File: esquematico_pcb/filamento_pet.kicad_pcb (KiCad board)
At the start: 2 copper layers, 150 x 50 mm, 31 parts, among them J1 01x02M, J10 01x03M, J11 01x02M, J12 01x04M, J13 01x02M, J2 01x02M, J3 01x02M, J4 01x02M, J5 01x02M, J6 01x03M, J7 01x03M, J8 01x02M, J9 01x04M, P1 Digital, P2 Analog, Q1 IRF540N, Q2 IRF540N

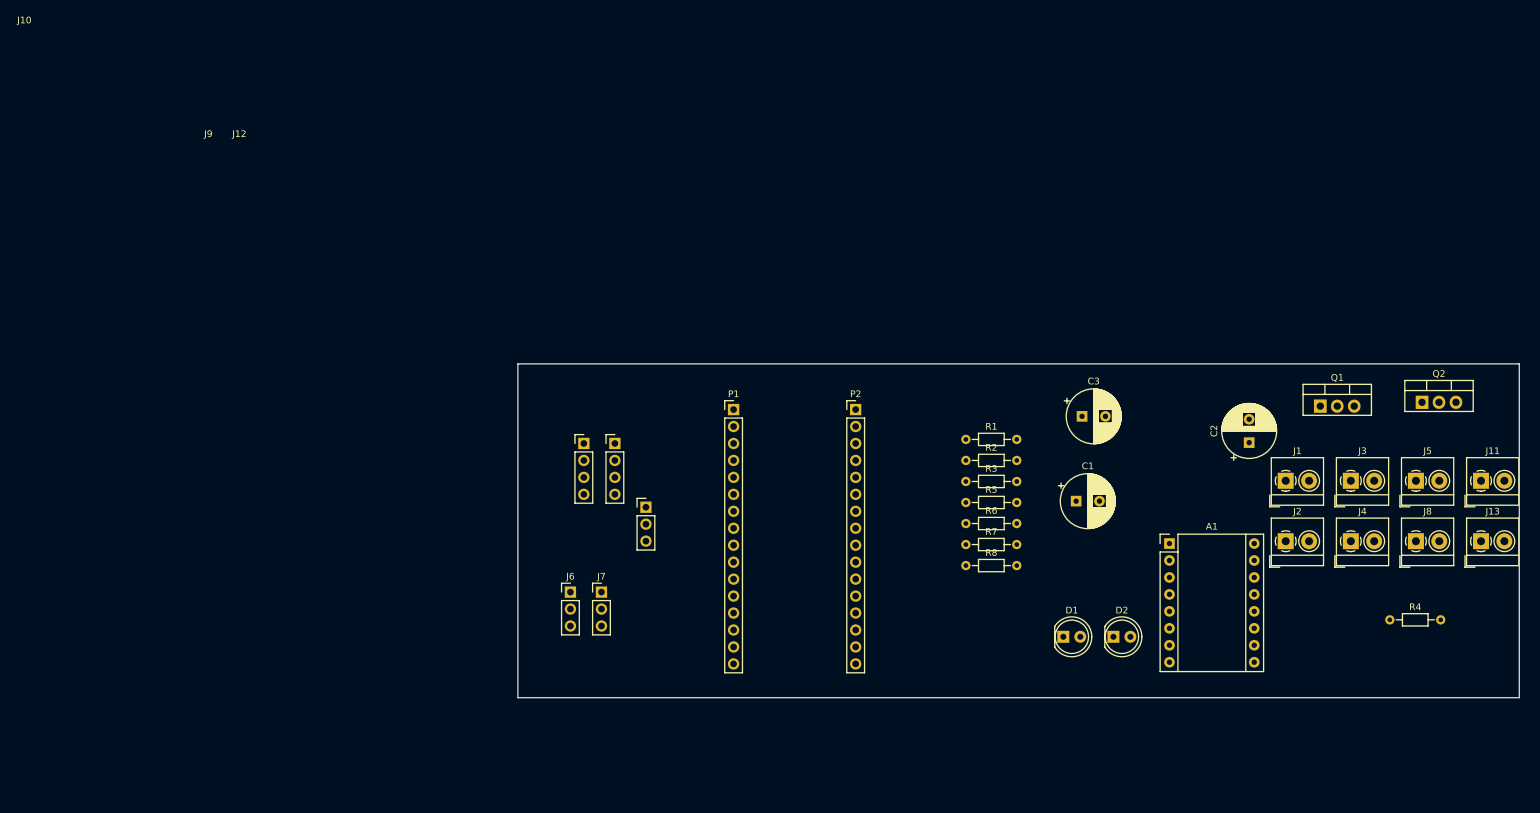
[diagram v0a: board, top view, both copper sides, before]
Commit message: Cambio de footprint Arduino Nano. Conector para encoder (Opcional). 2 Botones
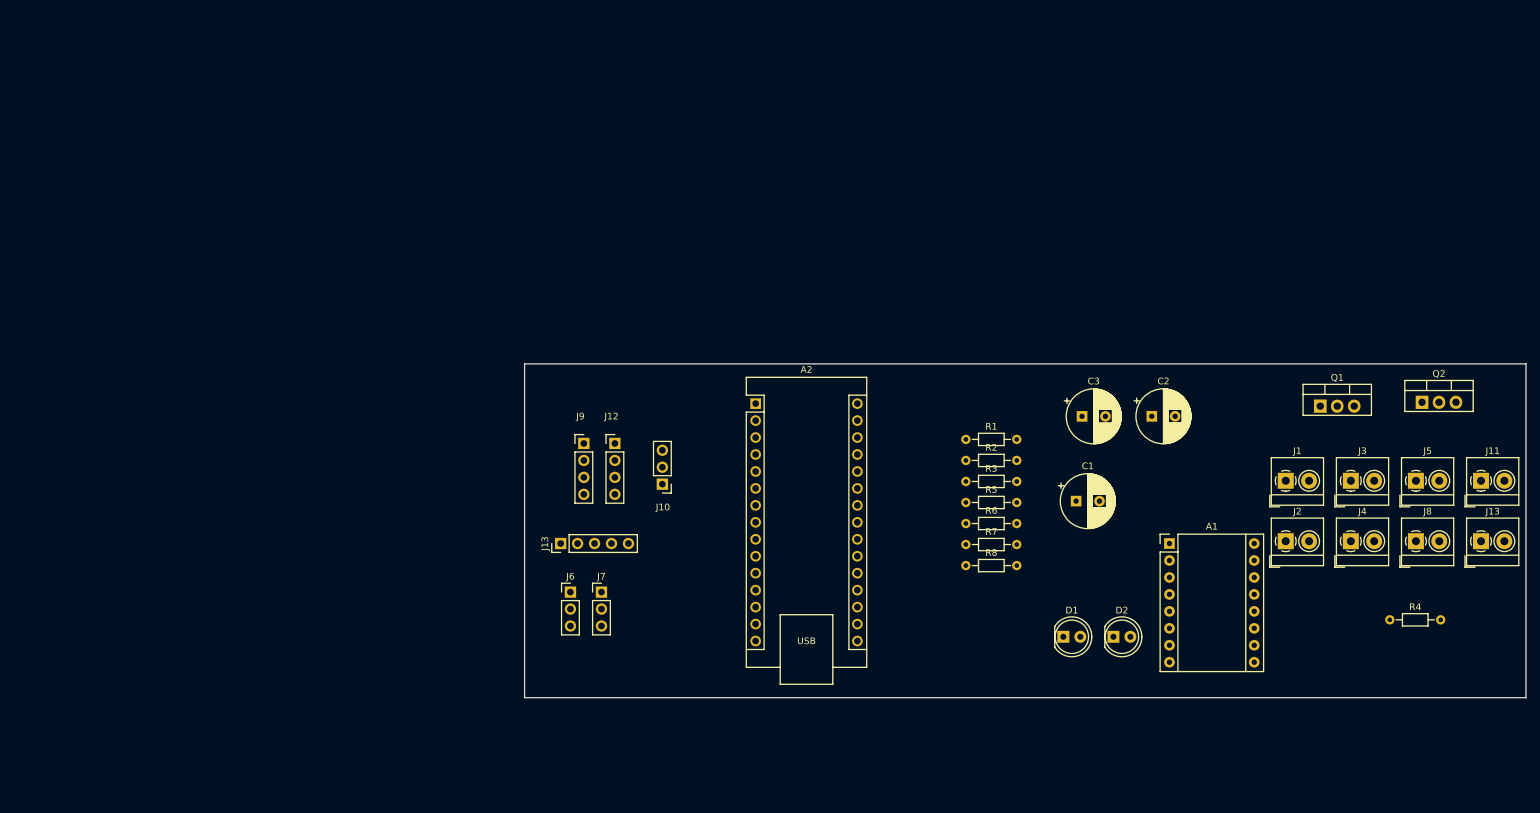
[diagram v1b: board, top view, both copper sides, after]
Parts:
- removed P1: Digital, Connector_PinHeader_2.54mm:PinHeader_1x16_P2.54mm_Vertical
- removed P2: Analog, Connector_PinHeader_2.54mm:PinHeader_1x16_P2.54mm_Vertical
- added A2: Arduino_Nano_v3.x, Module:Arduino_Nano, F.Cu at (54.6, 21.0)
- added J13: Conn_01x05_Pin, Connector_PinHeader_2.54mm:PinHeader_1x05_P2.54mm_Vertical, F.Cu at (25.4, 41.9)
- R1, R4: value R -> 1K8
- R2, R5: value R -> 10R
- R3, R6, R8: value R -> 10K
- R7: value R -> 4K7
- moved C2 15.1 mm to (113.9, 22.9), turned to 0 degrees
- moved J10 4.24 mm to (40.6, 33.0), turned to 180 degrees

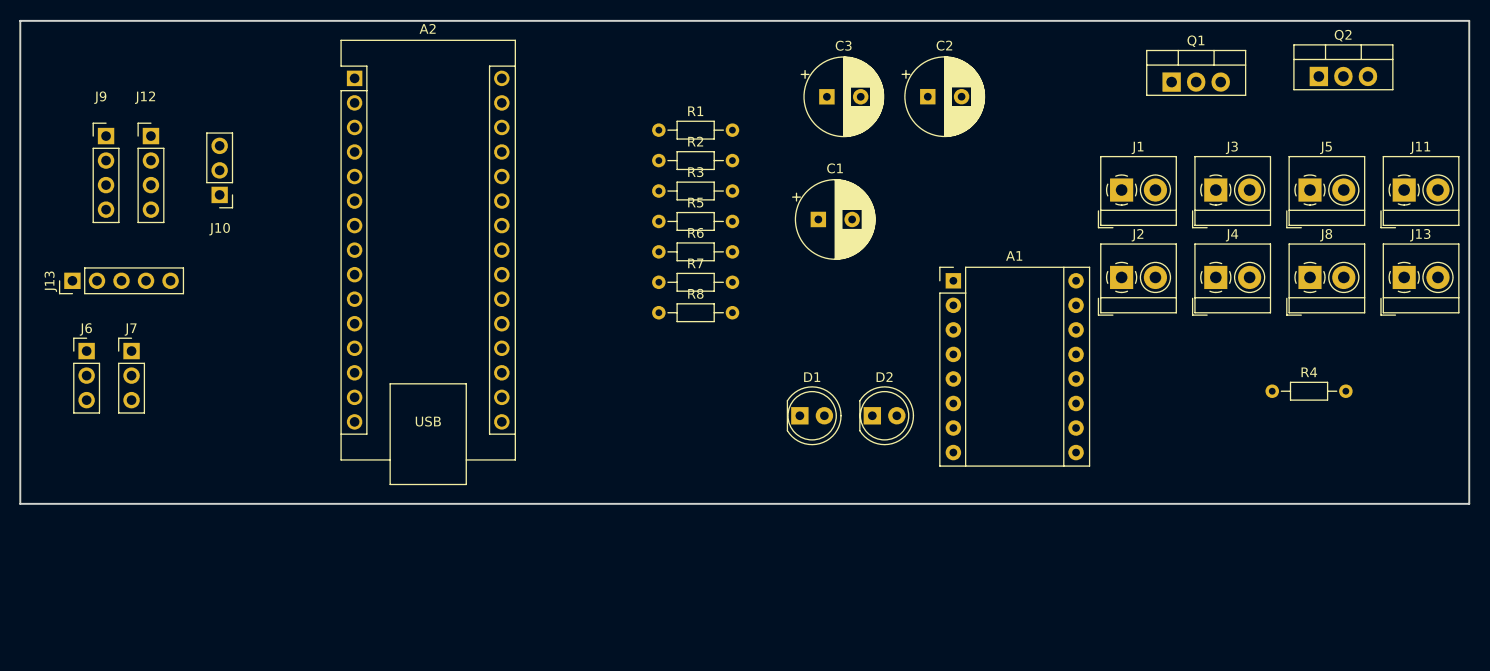
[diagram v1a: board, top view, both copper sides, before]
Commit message: PCB V1.0.0
Agregué LM7805
Cambios pequeños en el esquemático
V1.0.0 del PCB
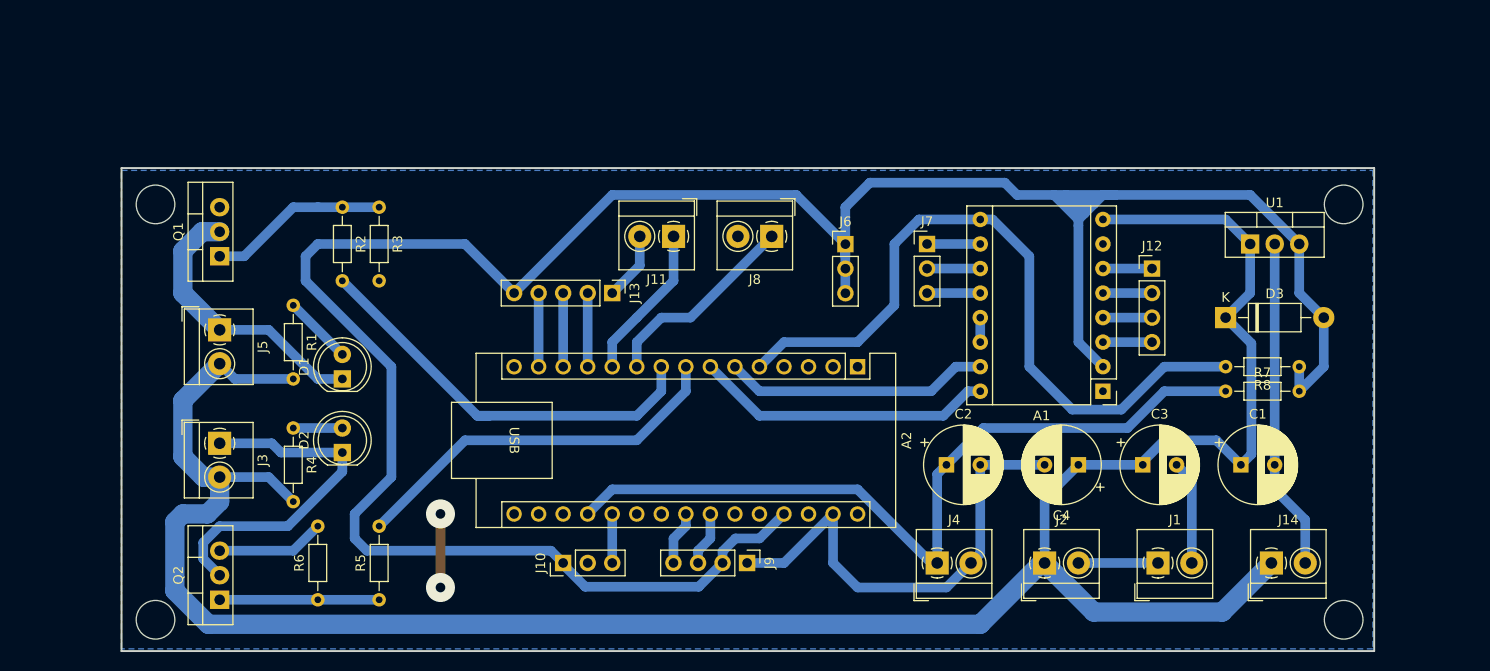
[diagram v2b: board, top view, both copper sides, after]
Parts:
- removed the J13 at (163.3, 41.6)
- removed the J13 at (25.4, 41.9)
- added C4: 10uf, Capacitor_THT:CP_Radial_D8.0mm_P3.50mm, F.Cu at (129.5, 61.0)
- added D3: 1N4007, Diode_THT:D_DO-41_SOD81_P10.16mm_Horizontal, F.Cu at (144.8, 45.7)
- added J13: Conn_01x05_Pin, Connector_PinHeader_2.54mm:PinHeader_1x05_P2.54mm_Vertical, F.Cu at (81.3, 43.2)
- added J14: 01x02M, TerminalBlock_4Ucon:TerminalBlock_4Ucon_1x02_P3.50mm_Horizontal, F.Cu at (149.5, 71.1)
- added U1: LM7805_TO220, Package_TO_SOT_THT:TO-220-3_Vertical, F.Cu at (147.3, 38.1)
- moved Q2 126.0 mm to (40.6, 74.9), turned to 90 degrees
- moved J5 113.8 mm to (40.6, 47.0), turned to -90 degrees
- moved J3 106.4 mm to (40.6, 58.7), turned to -90 degrees
- moved J12 104.5 mm to (137.2, 40.6)
- moved R4 101.4 mm to (48.3, 57.1), turned to -90 degrees
- moved Q1 100.2 mm to (40.6, 39.4), turned to 90 degrees
- moved J7 83.1 mm to (113.9, 38.1)
- moved J9 79.7 mm to (95.2, 71.1), turned to -90 degrees
- moved J6 79.3 mm to (105.4, 38.1)
- moved J11 75.8 mm to (87.6, 37.3), turned to 180 degrees
- moved R8 66.5 mm to (152.4, 50.8), turned to 180 degrees
- moved A2 60.0 mm to (106.7, 50.8), turned to -90 degrees
- moved R7 59.7 mm to (144.8, 53.3)
- moved J8 55.9 mm to (97.8, 37.3), turned to 180 degrees
- moved D2 55.0 mm to (53.3, 59.7), turned to 90 degrees
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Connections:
- A2 pad 4: GND -> unconnected-(A2-GND-Pad4)
- A2 pad 8: MOS -> FAN
- A2 pad 9: FAN -> MOS
- J10 pad 2: Pote_vel -> GND
- J10 pad 3: GND -> Pote_vel
- J11 pad 1: GND -> BUT2
- J11 pad 2: BUT2 -> GND
- J3 pad 1: Net-(D1-K) -> Net-(D2-K)
- J5 pad 1: Net-(D2-K) -> Net-(D1-K)
- J8 pad 1: GND -> BUT1
- J8 pad 2: BUT1 -> GND
- J9 pad 3: SDA -> SCL
- J9 pad 4: SCL -> SDA
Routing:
- net +5V: track 0.00 -> 259.8 mm
- net +12V: track 0.00 -> 242.3 mm
- net GND: track 0.00 -> 120.7 mm, vias 0 -> 2
- net Thermistor: track 0.00 -> 83.4 mm
- net EN: track 0.00 -> 75.0 mm
- net MOS: track 0.00 -> 43.7 mm
- net FAN: track 0.00 -> 40.1 mm
- net Net-(D2-K): track 0.00 -> 36.6 mm
- net DIR: track 0.00 -> 31.1 mm
- net Net-(D1-K): track 0.00 -> 29.2 mm
- net STEP: track 0.00 -> 27.5 mm
- net BUT1: track 0.00 -> 21.1 mm
- net Net-(Q1-G): track 0.00 -> 18.6 mm
- net Net-(Q2-G): track 0.00 -> 16.5 mm
- net BUT2: track 0.00 -> 16.1 mm
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- added copper zone on B.Cu, net GND
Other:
- board size 150 x 50 mm -> 129.7 x 50 mm
- board text added: "PCB_001"
- board text added: "V1.0.0"

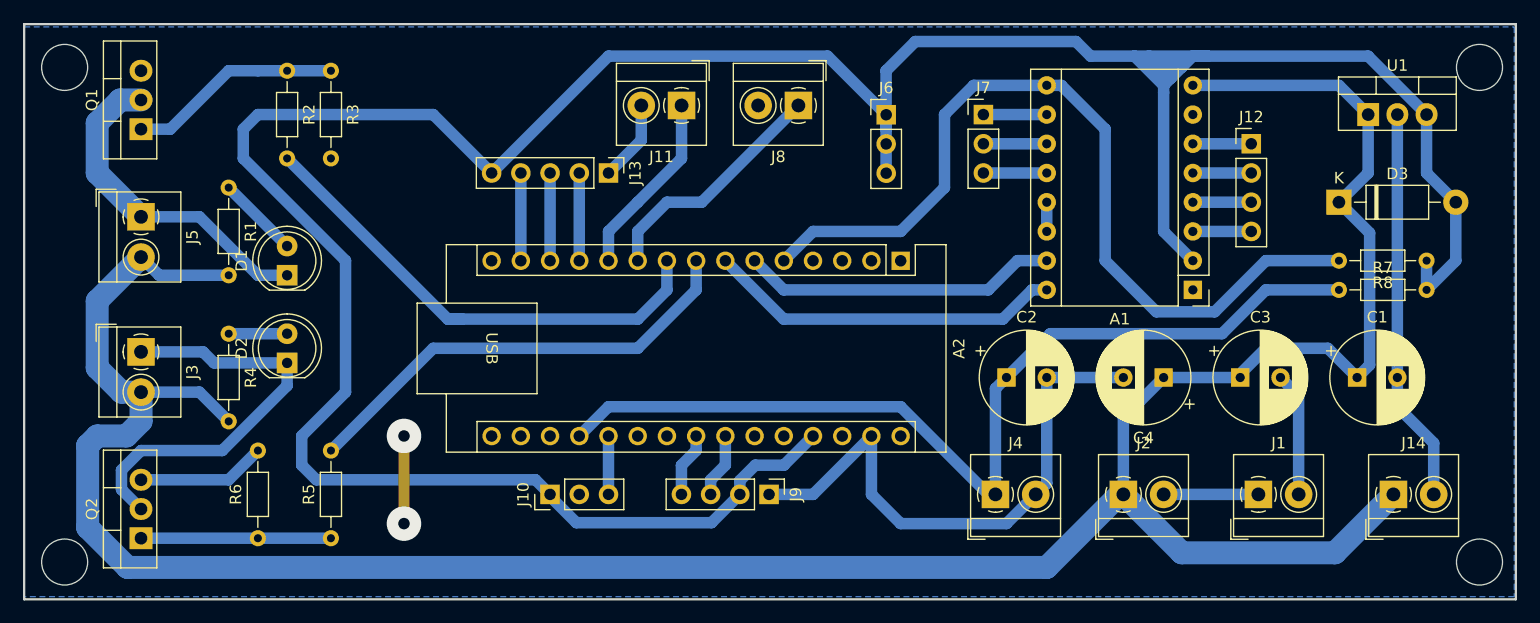
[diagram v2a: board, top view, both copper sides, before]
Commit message: Cambios recomendados por gonza
Hice varios cambios, agregué más puntes para que el power plane del GND sea mejor, Gonza comentó de agregar resistencias de pull down en las entradas de MSI del pololu, estas eran para controlar el stepper
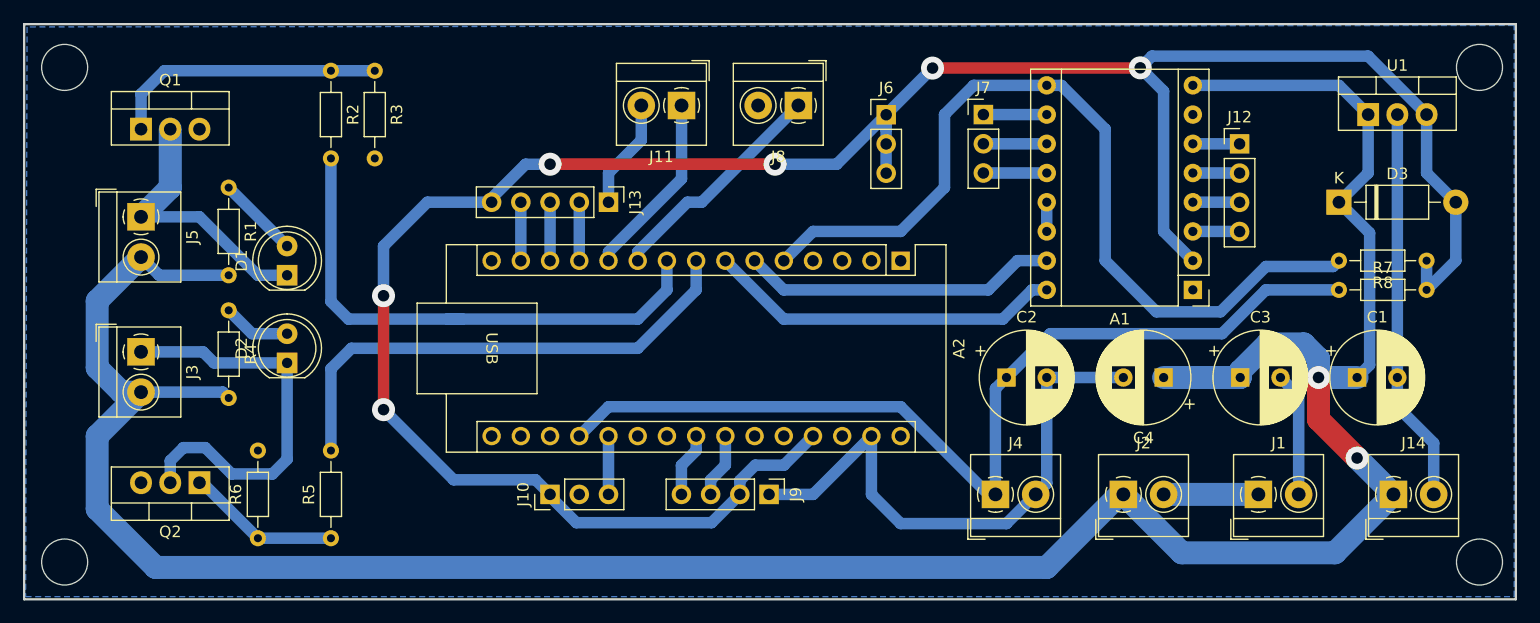
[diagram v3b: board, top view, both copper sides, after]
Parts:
- moved Q2 7.01 mm to (45.7, 70.1), turned to 180 degrees
- moved R3 3.81 mm to (61.0, 34.3)
- moved R2 3.81 mm to (57.1, 34.3)
- moved J13 2.54 mm to (81.3, 45.7)
- moved R4 2.03 mm to (48.3, 55.1)
- moved J12 1.02 mm to (136.1, 40.6)
- turned Q1 to 0 degrees
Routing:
- net +5V: track 259.8 -> 204.1 mm, vias 0 -> 6
- net GND: track 120.7 -> 104.4 mm, vias 2 -> 0
- net Net-(D1-K): track 29.2 -> 23.5 mm
- net Net-(Q1-G): track 18.6 -> 24.2 mm
- net FAN: track 40.1 -> 44.2 mm
- net MOS: track 43.7 -> 47.1 mm
- net Net-(Q2-G): track 16.5 -> 13.4 mm
- net SW: track 7.63 -> 5.09 mm
- net ENCB: track 7.63 -> 5.09 mm
- net ENCA: track 7.63 -> 5.09 mm
- net +12V: track 242.3 -> 240.8 mm, vias 0 -> 2
- net Net-(D2-K): track 36.6 -> 35.5 mm
- net BUT1: track 21.1 -> 20.0 mm
- net Net-(A1-2B): track 5.08 -> 4.07 mm
- net Net-(A1-2A): track 5.08 -> 4.07 mm
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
